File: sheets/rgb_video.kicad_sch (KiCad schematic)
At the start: 51 parts, among them CN3 DIN-8, U32 CXA1145P

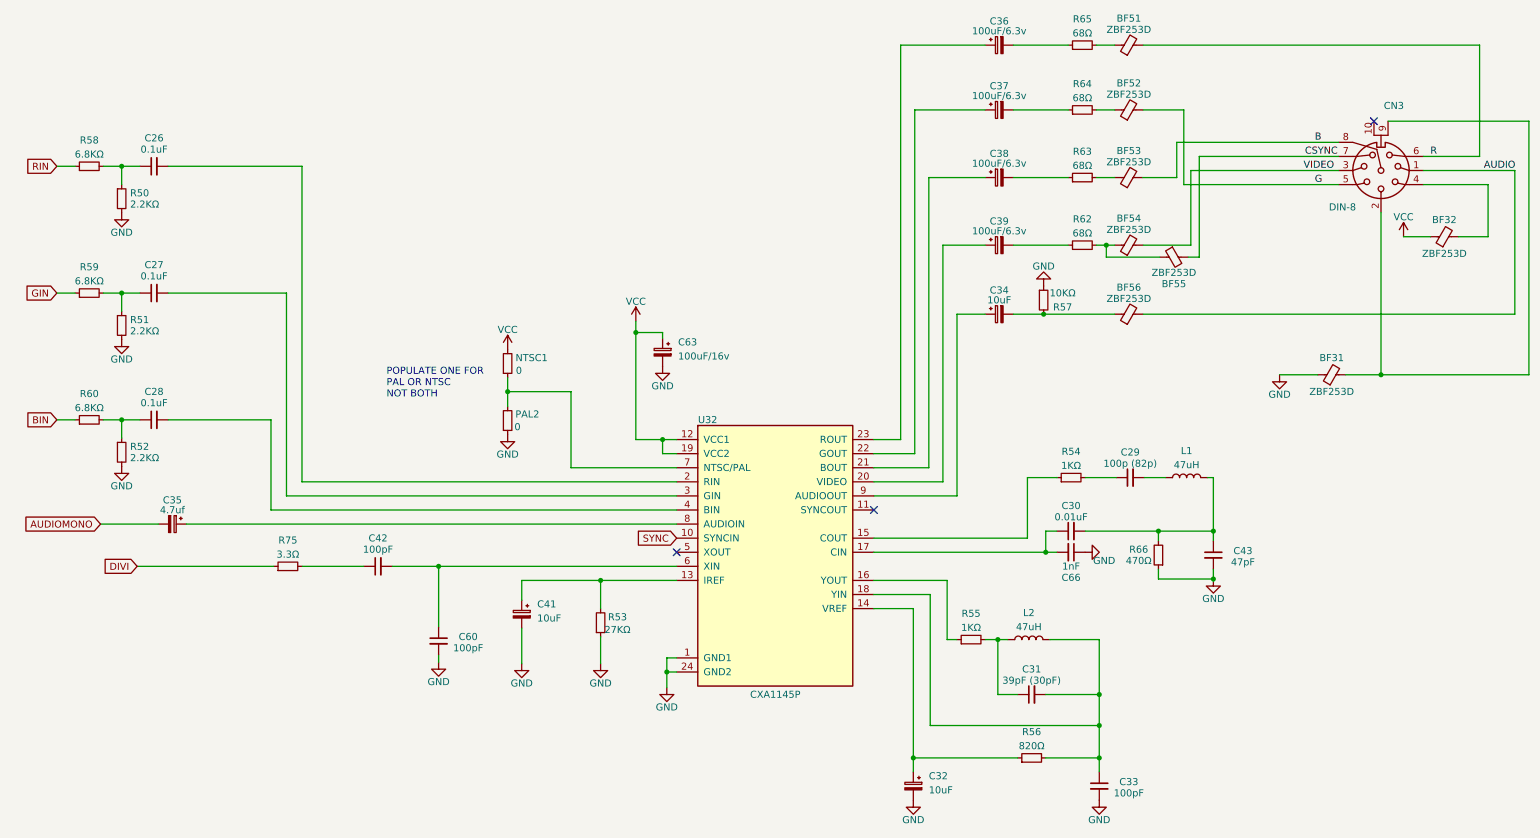
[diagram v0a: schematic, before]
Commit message: Silkscreen layout updates
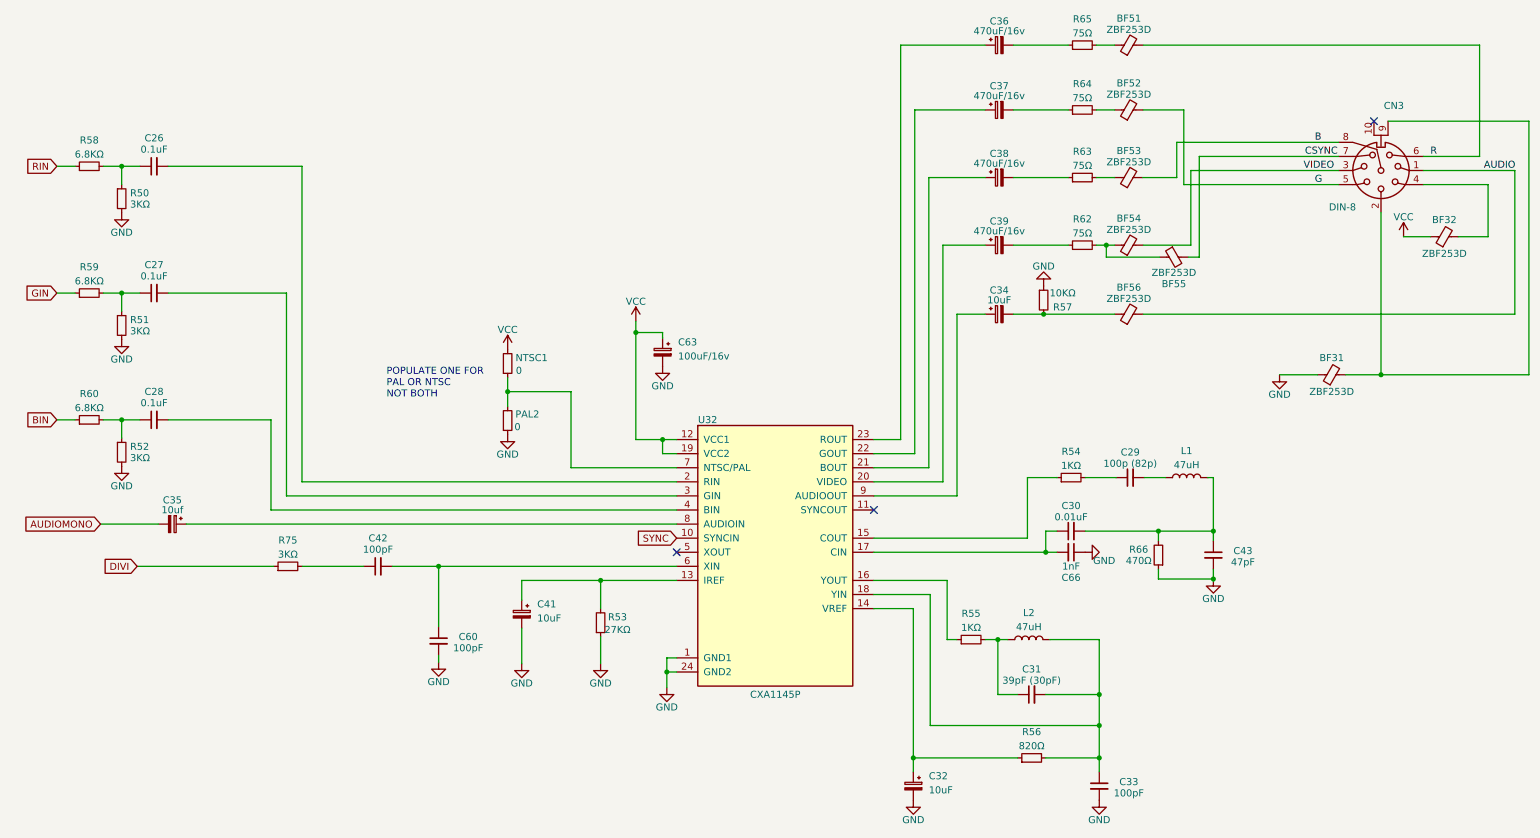
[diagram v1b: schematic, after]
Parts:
- C35: value 4.7uf -> 10uf
- C36, C37, C38, C39: value 100uF/6.3v -> 470uF/16v
- R50, R51, R52: value 2.2KΩ -> 3KΩ
- R62, R63, R64, R65: value 68Ω -> 75Ω
- R75: value 3.3Ω -> 3KΩ
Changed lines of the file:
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@@
       (effects (font (size 1.27 1.27)))
     )
-    (property "Value" "68Ω" (at 268.478 110.617 90)
+    (property "Value" "75Ω" (at 268.478 110.617 90)
       (effects (font (size 1.27 1.27)))
     )
@@
       (effects (font (size 1.27 1.27)) (justify left))
     )
-    (property "Value" "2.2KΩ" (at 96.774 128.27 0)
+    (property "Value" "3KΩ" (at 96.774 128.27 0)
       (effects (font (size 1.27 1.27)) (justify left))
     )
@@
       (effects (font (size 1.27 1.27)) (justify left))
     )
-    (property "Value" "2.2KΩ" (at 96.774 105.41 0)
+    (property "Value" "3KΩ" (at 96.774 105.41 0)
       (effects (font (size 1.27 1.27)) (justify left))
     )
@@
       (effects (font (size 1.27 1.27)))
     )
-    (property "Value" "68Ω" (at 268.478 98.425 90)
+    (property "Value" "75Ω" (at 268.478 98.425 90)
       (effects (font (size 1.27 1.27)))
     )
@@
       (effects (font (size 1.27 1.27)))
     )
-    (property "Value" "68Ω" (at 268.478 86.233 90)
+    (property "Value" "75Ω" (at 268.478 86.233 90)
       (effects (font (size 1.27 1.27)))
     )
@@
       (effects (font (size 1.27 1.27)))
     )
-    (property "Value" "4.7uf" (at 104.394 160.528 90)
+    (property "Value" "10uf" (at 104.394 160.528 90)
       (effects (font (size 1.27 1.27)))
     )
@@
       (effects (font (size 1.27 1.27)) (justify left))
     )
-    (property "Value" "2.2KΩ" (at 96.774 151.13 0)
+    (property "Value" "3KΩ" (at 96.774 151.13 0)
       (effects (font (size 1.27 1.27)) (justify left))
     )
@@
       (effects (font (size 1.27 1.27)))
     )
-    (property "Value" "100uF/6.3v" (at 253.492 110.236 90)
+    (property "Value" "470uF/16v" (at 253.492 110.236 90)
       (effects (font (size 1.27 1.27)))
     )
@@
       (effects (font (size 1.27 1.27)))
     )
-    (property "Value" "100uF/6.3v" (at 253.492 74.168 90)
+    (property "Value" "470uF/16v" (at 253.492 74.168 90)
       (effects (font (size 1.27 1.27)))
     )
@@
       (effects (font (size 1.27 1.27)))
     )
-    (property "Value" "3.3Ω" (at 125.222 168.529 90)
+    (property "Value" "3KΩ" (at 125.222 168.529 90)
       (effects (font (size 1.27 1.27)))
     )
@@
       (effects (font (size 1.27 1.27)))
     )
-    (property "Value" "100uF/6.3v" (at 253.492 98.044 90)
+    (property "Value" "470uF/16v" (at 253.492 98.044 90)
       (effects (font (size 1.27 1.27)))
     )
@@
       (effects (font (size 1.27 1.27)))
     )
-    (property "Value" "100uF/6.3v" (at 253.492 85.852 90)
+    (property "Value" "470uF/16v" (at 253.492 85.852 90)
       (effects (font (size 1.27 1.27)))
     )
@@
       (effects (font (size 1.27 1.27)))
     )
-    (property "Value" "68Ω" (at 268.478 74.549 90)
-      (effects (font (size 1.27 1.27)))
-    )
+    (property "Value" "75Ω" (at 268.478 74.549 90)
+      (effects (font (size 1.27 1.27)))
+    )

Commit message: Final update to Schematics Footprints Silkscreens
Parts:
- C63: value 100uF/16v -> 100nF; symbol Device:C_Polarized_Small -> Device:C_Small
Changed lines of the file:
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@@
     )
   )
-  (symbol (lib_id "Device:C_Polarized_Small") (at 192.786 132.08 0) (mirror y) (unit 1)
+  (symbol (lib_id "Device:C_Small") (at 192.786 132.08 0) (mirror y) (unit 1)
     (in_bom yes) (on_board yes) (dnp no) (fields_autoplaced)
-    (property "Reference" "C63" (at 195.58 130.2638 0)
+    (property "Reference" "C63" (at 195.58 130.8989 0)
       (effects (font (size 1.27 1.27)) (justify right))
     )
-    (property "Value" "100uF/16v" (at 195.58 132.8038 0)
+    (property "Value" "100nF" (at 195.58 133.4389 0)
       (effects (font (size 1.27 1.27)) (justify right))
     )

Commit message: Some tweaks
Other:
- company: (none) -> SNK
- title: (none) -> NeoGeo AES
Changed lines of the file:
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@@
 (kicad_sch (version 20230121) (generator eeschema)
   (paper "A3")
+  (title_block
+    (title "NeoGeo AES")
+    (date "2023-08-19")
+    (rev "3.5")
+    (company "SNK")
+    (comment 3 "https://github.com/Board-Folk")
+    (comment 4 "Recreated By The Board Folk Team")
+  )
   (junction (at 192.786 147.828) (diameter 0) (color 0 0 0 0)
   )

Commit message: Updates to PCB Move P2 Joystick Port Move Memory Card Move Holes at top right Silkscreen added Update Titles
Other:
- title: NeoGeo AES -> NeoGeo AES 3-5
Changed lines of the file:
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@@
   (paper "A3")
   (title_block
-    (title "NeoGeo AES")
-    (date "2023-08-19")
-    (rev "3.5")
+    (title "NeoGeo AES 3-5")
+    (date "2023-08-27")
+    (rev "BF1.1")
     (company "SNK")
     (comment 3 "https://github.com/Board-Folk")

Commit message: More little tweaks
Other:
- note added: "N.F"
- note added: "POPULATE ONE FOR NTSC OR PAL NOT BOTH!!!"
- note removed: "POPULATE ONE FOR PAL OR NTSC NOT BOTH"
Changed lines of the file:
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@@
     (stroke (width 0) (type default))
   )
-  (text "POPULATE ONE FOR\nPAL OR NTSC\nNOT BOTH" (at 143.002 140.462 0)
+  (rectangle (start 140.462 126.238) (end 174.498 153.924)
+    (stroke (width 0) (type dash))
+    (fill (type none))
+  )
+  (rectangle (start 262.89 166.116) (end 274.828 176.022)
+    (stroke (width 0) (type dash))
+    (fill (type none))
+  )
+  (text "POPULATE ONE\nFOR\nNTSC OR PAL\nNOT BOTH!!!" (at 140.97 134.874 0)
     (effects (font (size 1.27 1.27)) (justify left bottom))
   )
+  (text "N.F" (at 264.922 175.514 0)
+    (effects (font (size 1.27 1.27)) (justify left bottom))
+  )

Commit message: Adding Mouser Part Numbers
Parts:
- BF31, BF32, BF51, BF52, BF53, BF54, BF55, BF56: Mouser (none) -> 80-B-06-R-25
- C26, C27, C28, C63: Mouser (none) -> 810-FG26C0G1H104JNT0
- C29: value 100p (82p) -> 100pF (82p); Mouser (none) -> 810-FG28C0G1H101JNT6
- C30: Mouser (none) -> 810-FG28C0G1H103JNT0
- C31: Mouser (none) -> 810-FG28C0G1H390JNT6
- C32, C34, C41: Mouser (none) -> 667-ECA-1CM100I
- C33, C42, C43, C60: Mouser (none) -> 810-FG28C0G1H101JNT6
- C35: value 10uf -> 10uF; Mouser (none) -> 667-ECA-1CM100I
- C66: Comment (none) -> Not Fitted; Mouser (none) -> 810-FG28C0G1H102JNT6

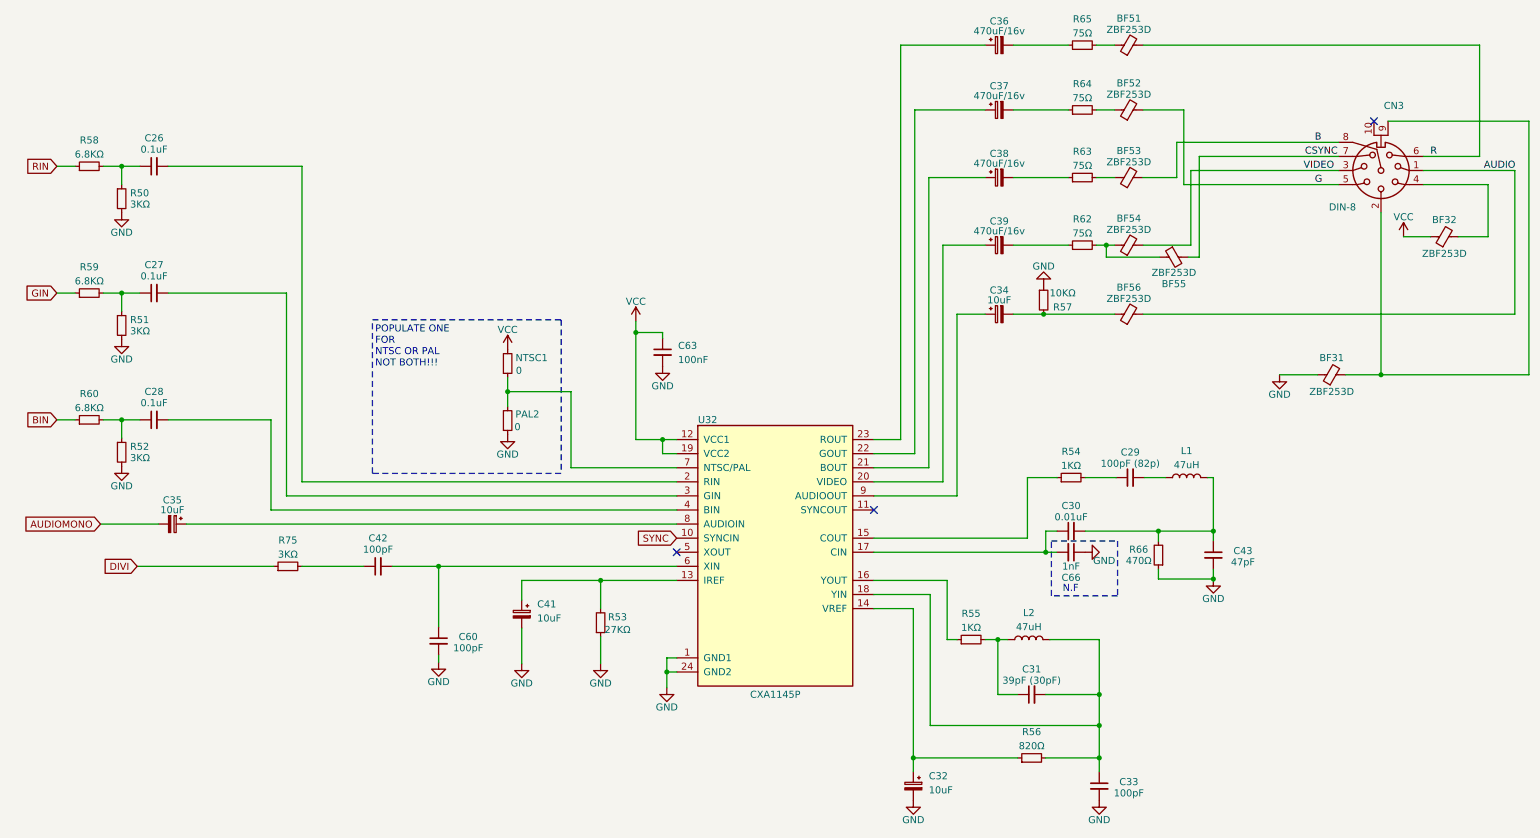
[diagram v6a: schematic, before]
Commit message: More silkscreen tidy up, adding mouser components to BOM
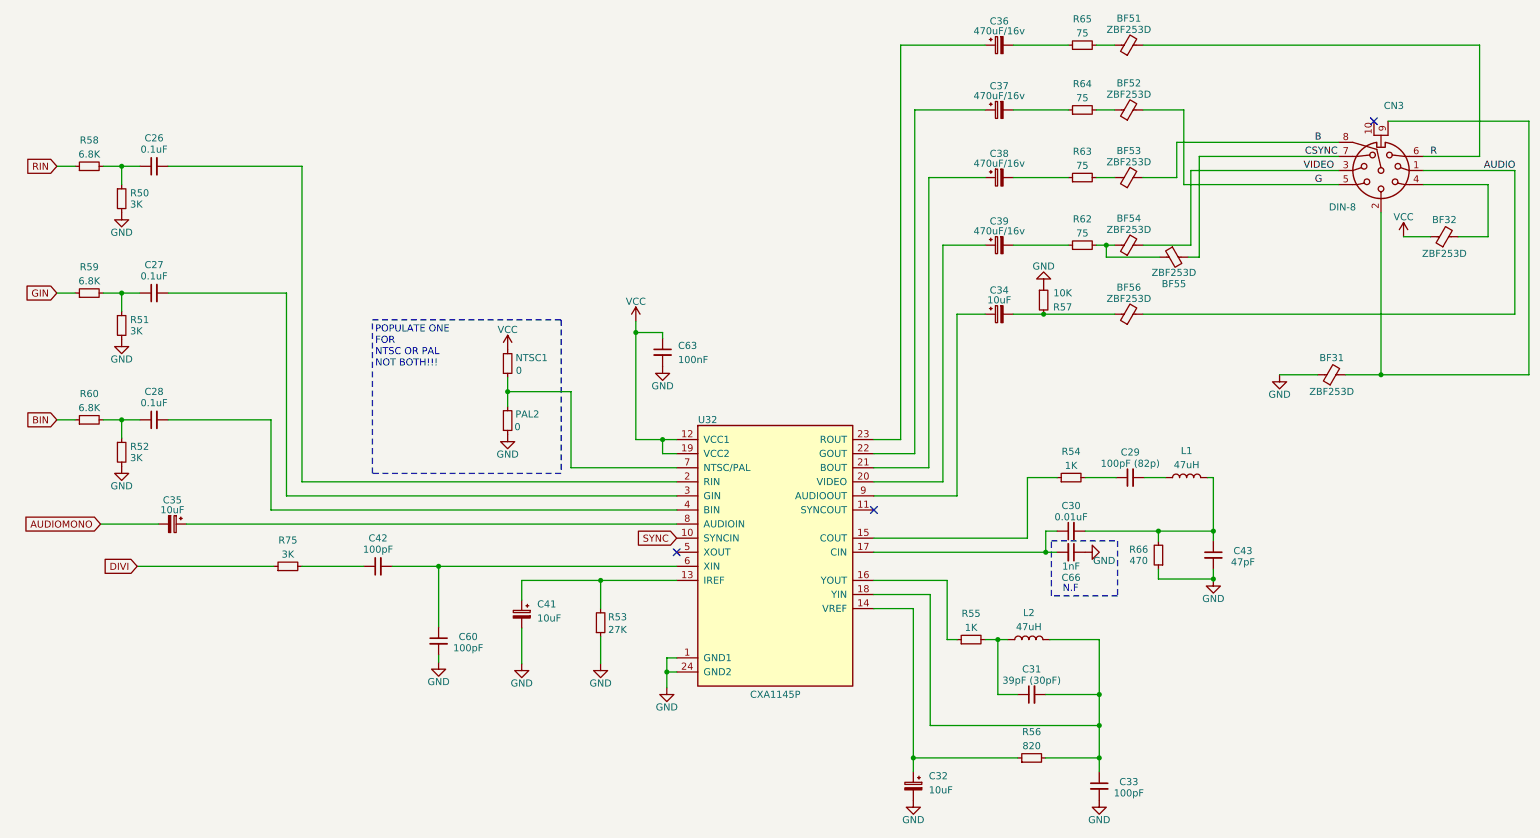
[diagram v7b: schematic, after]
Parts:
- C36, C37, C38, C39: Mouser (none) -> 647-UHE1C471MPD6
- L1, L2: Mouser (none) -> 530-SFAPI-470K-UL
- R50, R51, R52, R75: value 3KΩ -> 3K
- R53: value 27KΩ -> 27K
- R54, R55: value 1KΩ -> 1K
- R56: value 820Ω -> 820
- R57: value 10KΩ -> 10K
- R58, R59, R60: value 6.8KΩ -> 6.8K
- R62, R63, R64, R65: value 75Ω -> 75
- R66: value 470Ω -> 470
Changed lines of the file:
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@@
       (effects (font (size 1.27 1.27)))
     )
-    (property "Value" "75Ω" (at 268.478 110.617 90)
+    (property "Value" "75" (at 268.478 110.617 90)
       (effects (font (size 1.27 1.27)))
     )
@@
       (effects (font (size 1.27 1.27)) (justify left))
     )
-    (property "Value" "3KΩ" (at 96.774 128.27 0)
+    (property "Value" "3K" (at 96.774 128.27 0)
       (effects (font (size 1.27 1.27)) (justify left))
     )
@@
       (effects (font (size 1.27 1.27)) (justify left))
     )
-    (property "Value" "3KΩ" (at 96.774 105.41 0)
+    (property "Value" "3K" (at 96.774 105.41 0)
       (effects (font (size 1.27 1.27)) (justify left))
     )
@@
       (effects (font (size 1.27 1.27)))
     )
-    (property "Value" "75Ω" (at 268.478 98.425 90)
+    (property "Value" "75" (at 268.478 98.425 90)
       (effects (font (size 1.27 1.27)))
     )
@@
       (effects (font (size 1.27 1.27)))
     )
-    (property "Value" "6.8KΩ" (at 89.408 119.253 90)
+    (property "Value" "6.8K" (at 89.408 119.253 90)
       (effects (font (size 1.27 1.27)))
     )
@@
       (effects (font (size 1.27 1.27)))
     )
-    (property "Value" "75Ω" (at 268.478 86.233 90)
+    (property "Value" "75" (at 268.478 86.233 90)
       (effects (font (size 1.27 1.27)))
     )
@@
       (effects (font (size 1.27 1.27)))
     )
-    (property "Value" "6.8KΩ" (at 89.408 96.393 90)
+    (property "Value" "6.8K" (at 89.408 96.393 90)
       (effects (font (size 1.27 1.27)))
     )
@@
       (effects (font (size 1.27 1.27)) hide)
     )
-    (property "Mouser" "" (at 258.826 183.896 0)
+    (property "Mouser" "530-SFAPI-470K-UL" (at 258.826 183.896 0)
       (effects (font (size 1.27 1.27)) hide)
     )
@@
       (effects (font (size 1.27 1.27)))
     )
-    (property "Value" "1KΩ" (at 248.412 181.737 90)
+    (property "Value" "1K" (at 248.412 181.737 90)
       (effects (font (size 1.27 1.27)))
     )
@@
       (effects (font (size 1.27 1.27)))
     )
-    (property "Value" "820Ω" (at 259.334 203.073 90)
+    (property "Value" "820" (at 259.334 203.073 90)
       (effects (font (size 1.27 1.27)))
     )
@@
       (effects (font (size 1.27 1.27)) hide)
     )
-    (property "Mouser" "" (at 287.274 154.686 0)
+    (property "Mouser" "530-SFAPI-470K-UL" (at 287.274 154.686 0)
       (effects (font (size 1.27 1.27)) hide)
     )
@@
       (effects (font (size 1.27 1.27)))
     )
-    (property "Value" "1KΩ" (at 266.446 152.527 90)
+    (property "Value" "1K" (at 266.446 152.527 90)
       (effects (font (size 1.27 1.27)))
     )
@@
       (effects (font (size 1.27 1.27)))
     )
-    (property "Value" "27KΩ" (at 184.658 182.118 0)
+    (property "Value" "27K" (at 184.658 182.118 0)
       (effects (font (size 1.27 1.27)))
     )
@@
       (effects (font (size 1.27 1.27)))
     )
-    (property "Value" "470Ω" (at 278.638 169.672 0)
+    (property "Value" "470" (at 278.638 169.672 0)
       (effects (font (size 1.27 1.27)))
     )
@@
       (effects (font (size 1.27 1.27)) (justify left))
     )
-    (property "Value" "3KΩ" (at 96.774 151.13 0)
+    (property "Value" "3K" (at 96.774 151.13 0)
       (effects (font (size 1.27 1.27)) (justify left))
     )
@@
       (effects (font (size 1.27 1.27)))
     )
-    (property "Value" "6.8KΩ" (at 89.408 142.113 90)
+    (property "Value" "6.8K" (at 89.408 142.113 90)
       (effects (font (size 1.27 1.27)))
     )
@@
       (effects (font (size 1.27 1.27)) hide)
     )
-    (property "Mouser" "" (at 253.492 112.776 0)
+    (property "Mouser" "647-UHE1C471MPD6" (at 253.492 112.776 0)
       (effects (font (size 1.27 1.27)) hide)
     )
@@
       (effects (font (size 1.27 1.27)) hide)
     )
-    (property "Mouser" "" (at 253.492 76.708 0)
+    (property "Mouser" "647-UHE1C471MPD6" (at 253.492 76.708 0)
       (effects (font (size 1.27 1.27)) hide)
     )
@@
       (effects (font (size 1.27 1.27)))
     )
-    (property "Value" "3KΩ" (at 125.222 168.529 90)
+    (property "Value" "3K" (at 125.222 168.529 90)
       (effects (font (size 1.27 1.27)))
     )
@@
       (effects (font (size 1.27 1.27)) hide)
     )
-    (property "Mouser" "" (at 253.492 100.584 0)
+    (property "Mouser" "647-UHE1C471MPD6" (at 253.492 100.584 0)
       (effects (font (size 1.27 1.27)) hide)
     )
@@
       (effects (font (size 1.27 1.27)) hide)
     )
-    (property "Mouser" "" (at 253.492 88.392 0)
+    (property "Mouser" "647-UHE1C471MPD6" (at 253.492 88.392 0)
       (effects (font (size 1.27 1.27)) hide)
     )
@@
       (effects (font (size 1.27 1.27)))
     )
-    (property "Value" "10KΩ" (at 264.922 121.412 0)
+    (property "Value" "10K" (at 264.922 121.412 0)
       (effects (font (size 1.27 1.27)))
     )
@@
       (effects (font (size 1.27 1.27)))
     )
-    (property "Value" "75Ω" (at 268.478 74.549 90)
-      (effects (font (size 1.27 1.27)))
-    )
+    (property "Value" "75" (at 268.478 74.549 90)
+      (effects (font (size 1.27 1.27)))
+    )

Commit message: Little tweaks to silkscreen Updated BOM with mouser parts
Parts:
- C66: now left out of the parts list
- CN3, U32: Comment (none) -> Use Original
- NTSC1: Comment (none) -> Fit if NTSC; now left out of the parts list
- PAL2: Comment (none) -> Fit if PAL; now left out of the parts list
- R50, R51, R52, R75: Mouser (none) -> 71-RN60D3001F
- R53: Mouser (none) -> 71-RN60D-F-27K
- R54, R55: Mouser (none) -> 71-CMF501K0000FHEA
- R56: Mouser (none) -> 71-RN60D8200F
- R57: Mouser (none) -> 71-RN60E1002F
- R58, R59, R60: Mouser (none) -> 71-RN60D6801F
- R62, R63, R64, R65: Mouser (none) -> 71-CMF5075R000FHEB
- R66: Mouser (none) -> 71-RN60C4700F
